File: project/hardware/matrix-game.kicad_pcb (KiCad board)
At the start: 2 copper layers, 100 x 100 mm, 32 parts, among them SW1 button_center, SW2 button_left, SW3 button_down, SW4 button_right, SW5 button_up, U1 NUCLEO-F042K6, U2 MAX7219, U3 DM-OLED096-636

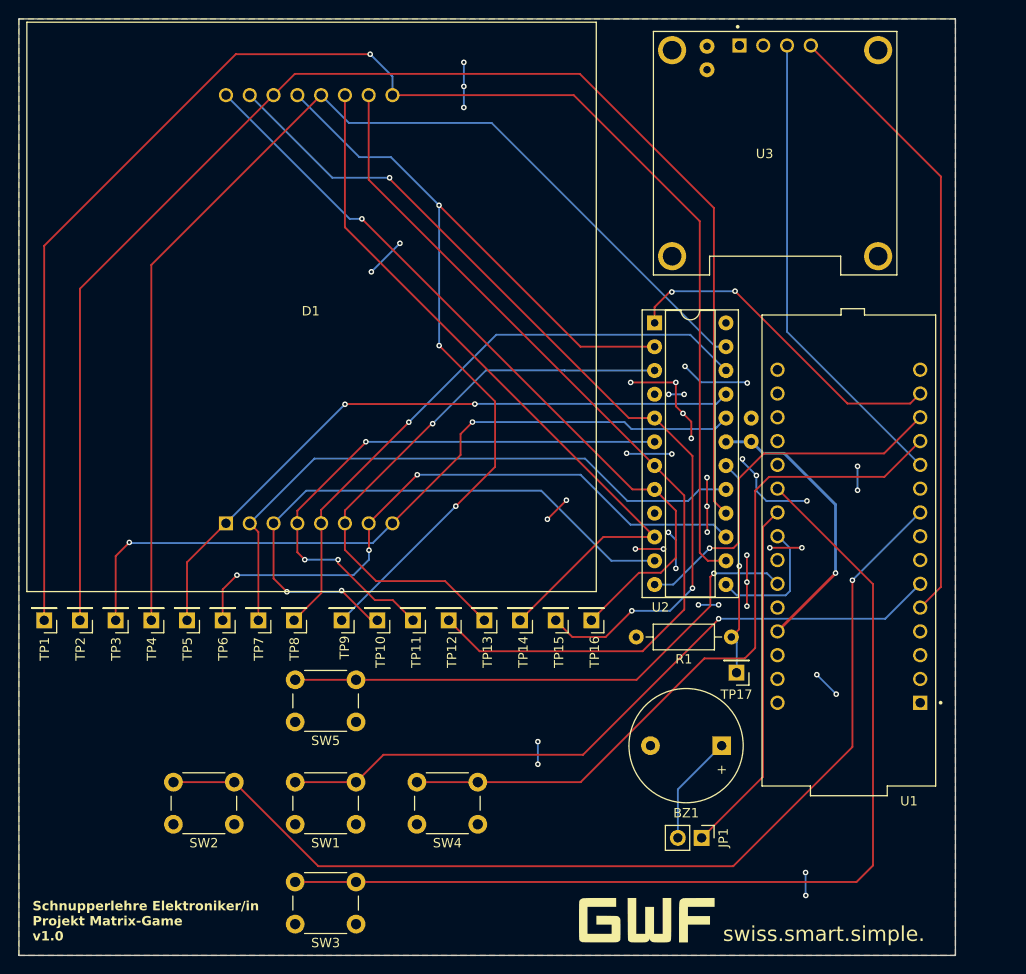
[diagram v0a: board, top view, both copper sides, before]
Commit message: [project/hardware] fix: wrong connection of R1
R1 was wrongly connectet to GND instead of +5V
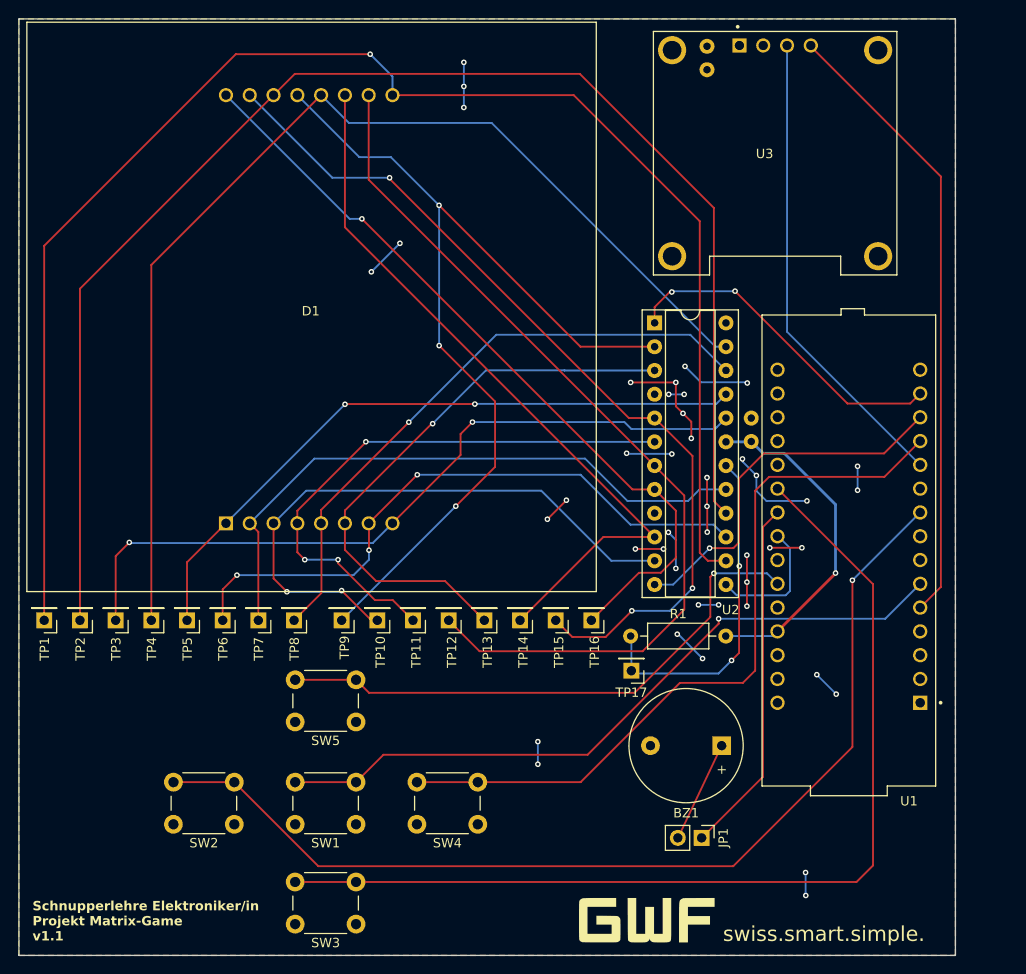
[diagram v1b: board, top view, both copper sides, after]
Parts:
- R1: value 10k -> 22k
- moved TP17 11.2 mm to (155.4, 114.6)
- moved R1 10.8 mm to (155.3, 110.9), turned to 0 degrees
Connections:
- R1 pad 2: GND -> +5V
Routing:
- net Net-(U2-ISET): track 22.7 -> 37.0 mm, vias 1 -> 2
- net Net-(BZ1-+): track 12.3 -> 0.54 mm
- net +5V: track 30.6 -> 36.3 mm
- net GND: track 49.7 -> 53.5 mm, vias 26 -> 28
- net button_up: track 58.5 -> 60.3 mm
- net button_right: track 78.7 -> 80.1 mm
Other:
- board text added: "Schnupperlehre Elektroniker/in Projekt Matrix-Game v1.1"
- board text removed: "Schnupperlehre Elektroniker/in Projekt Matrix-Game v1.0"

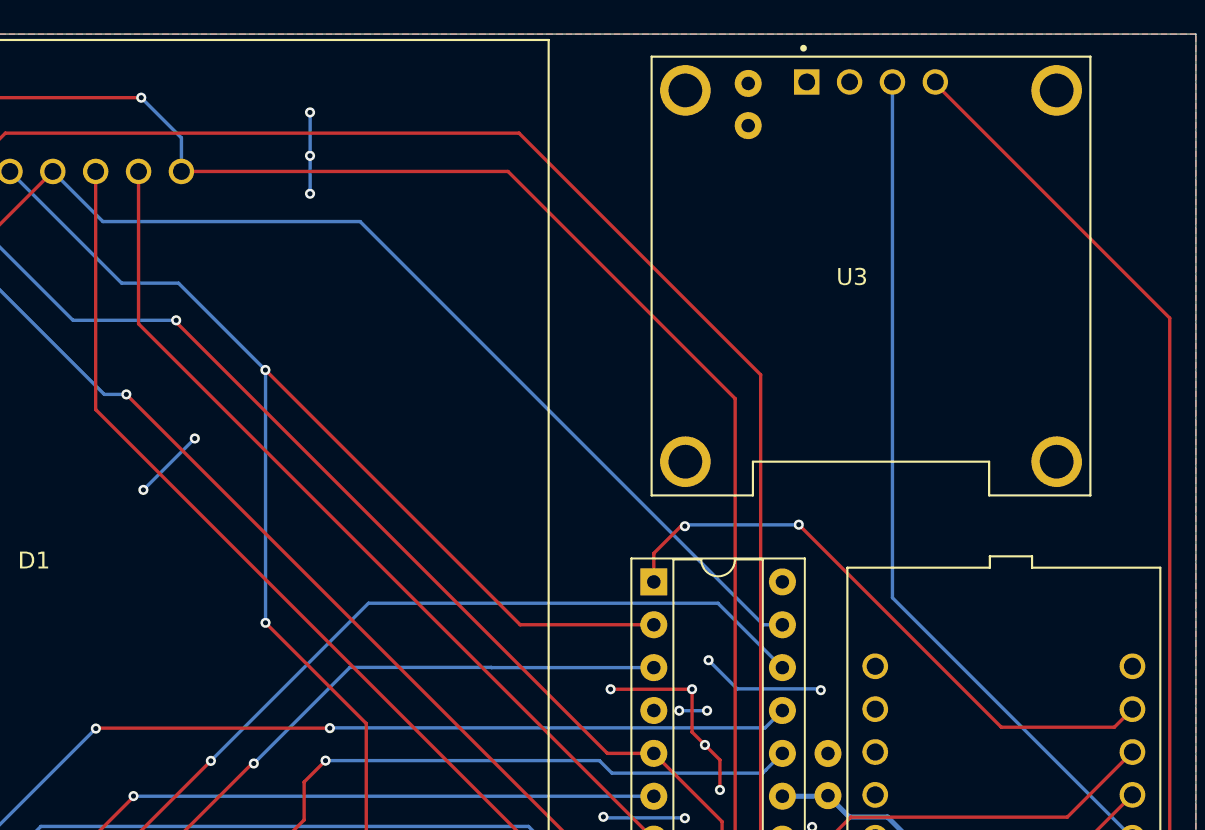
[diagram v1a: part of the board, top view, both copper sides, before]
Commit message: [project/hardware] fix: footprint of LCD
Adjusted mouting hole distances:

- previous[mm]: 22x22
- now[mm]: 23.5x23.8
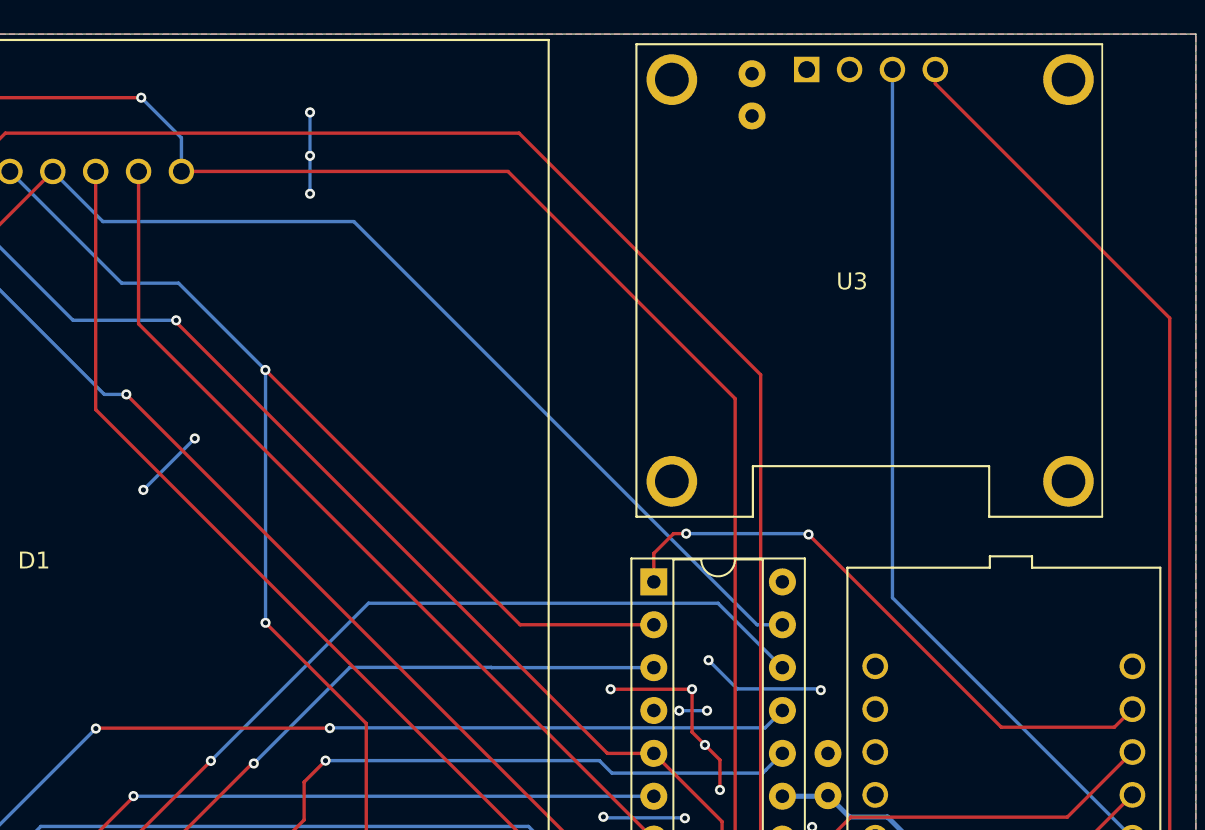
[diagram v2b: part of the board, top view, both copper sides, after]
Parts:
- moved C1 0.62 mm to (163.7, 49.9)
- moved U3 0.26 mm to (170.8, 59.6)
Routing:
- net max_mosi: track 36.4 -> 35.9 mm
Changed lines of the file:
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@@
 	(footprint "DM-OLED096-636:MODULE_DM-OLED096-636"
 		(layer "F.Cu")
-		(at 170.75 59.3375)
+		(at 170.75 59.6)
 		(property "Reference" "U3"
 			(at -1.125 0.0625 0)
@@
 		(attr through_hole)
 		(fp_line
-			(start -13 -13)
-			(end 13 -13)
+			(start -13.9 -14)
+			(end 13.7 -14)
 			(stroke
 				(width 0.127)
@@
 		)
 		(fp_line
-			(start -13 13)
-			(end -13 -13)
+			(start -13.9 14)
+			(end -13.9 -14)
 			(stroke
 				(width 0.127)
@@
 		(fp_line
 			(start -7 11)
-			(end -7 13)
+			(end -7 14)
 			(stroke
 				(width 0.127)
@@
 		)
 		(fp_line
-			(start -7 13)
-			(end -13 13)
+			(start -7 14)
+			(end -13.9 14)
 			(stroke
 				(width 0.127)
@@
 		)
 		(fp_line
-			(start 7 13)
+			(start 7 14)
 			(end 7 11)
 			(stroke
@@
 		)
 		(fp_line
-			(start 13 -13)
-			(end 13 13)
+			(start 13.7 14)
+			(end 7 14)
 			(stroke
 				(width 0.127)
@@
 		)
 		(fp_line
-			(start 13 13)
-			(end 7 13)
+			(start 13.7 14)
+			(end 13.7 -14)
 			(stroke
-				(width 0.127)
-				(type solid)
-			)
-			(layer "F.SilkS")
-		)
-		(fp_circle
-			(center -4 -13.5)
-			(end -3.9 -13.5)
-			(stroke
-				(width 0.2)
-				(type solid)
+				(width 0.1)
+				(type default)
 			)
-			(fill none)
 			(layer "F.SilkS")
 		)
 		(fp_line
-			(start -13.25 -13.25)
-			(end 13.25 -13.25)
+			(start -13.9 -14)
+			(end 13.7 -14)
 			(stroke
 				(width 0.05)
@@
 		)
 		(fp_line
-			(start -13.25 13.25)
-			(end -13.25 -13.25)
+			(start -13.9 14)
+			(end -13.9 -14)
 			(stroke
 				(width 0.05)
@@
 		)
 		(fp_line
-			(start 13.25 -13.25)
-			(end 13.25 13.25)
+			(start 13.7 -14)
+			(end 13.7 14)
 			(stroke
 				(width 0.05)
@@
 		)
 		(fp_line
-			(start 13.25 13.25)
-			(end -13.25 13.25)
+			(start 13.7 14)
+			(end -13.9 14)
 			(stroke
 				(width 0.05)
@@
 		)
 		(fp_line
-			(start -13 -13)
-			(end 13 -13)
+			(start -13.9 -14)
+			(end 13.7 -14)
 			(stroke
 				(width 0.127)
@@
 		)
 		(fp_line
-			(start -13 13)
-			(end -13 -13)
+			(start -13.9 14)
+			(end -13.9 -14)
 			(stroke
 				(width 0.127)
@@
 		)
 		(fp_line
-			(start -7 13)
-			(end -13 13)
+			(start -7 14)
+			(end -13.9 14)
 			(stroke
 				(width 0.127)
@@
 		)
 		(fp_line
-			(start -7 13)
+			(start -7 14)
 			(end -7 11)
 			(stroke
@@
 		(fp_line
 			(start 7 11)
-			(end 7 13)
+			(end 7 14)
 			(stroke
 				(width 0.127)
@@
 		)
 		(fp_line
-			(start 13 -13)
-			(end 13 13)
+			(start 13.7 -14)
+			(end 13.7 14)
 			(stroke
 				(width 0.127)
@@
 		)
 		(fp_line
-			(start 13 13)
-			(end 7 13)
+			(start 13.7 14)
+			(end 7 14)
 			(stroke
 				(width 0.127)
@@
 		)
 		(pad "1" thru_hole rect
-			(at -3.81 -11.5)
+			(at -3.81 -12.5)
 			(size 1.508 1.508)
 			(drill 1)
@@
 		)
 		(pad "2" thru_hole circle
-			(at -1.27 -11.5)
+			(at -1.27 -12.5)
 			(size 1.508 1.508)
 			(drill 1)
@@
 		)
 		(pad "3" thru_hole circle
-			(at 1.27 -11.5)
+			(at 1.27 -12.5)
 			(size 1.508 1.508)
 			(drill 1)
@@
 		)
 		(pad "4" thru_hole circle
-			(at 3.81 -11.5)
+			(at 3.81 -12.5)
 			(size 1.508 1.508)
 			(drill 1)
@@
 		)
 		(pad "S1" thru_hole circle
-			(at -11 -11)
+			(at -11.8 -11.9)
 			(size 3 3)
 			(drill 2)
@@
 		)
 		(pad "S2" thru_hole circle
-			(at 11 -11)
+			(at 11.7 -11.9)
 			(size 3 3)
 			(drill 2)
@@
 		)
 		(pad "S3" thru_hole circle
-			(at 11 11)
+			(at 11.7 11.9)
 			(size 3 3)
 			(drill 2)
@@
 		)
 		(pad "S4" thru_hole circle
-			(at -11 11)
+			(at -11.8 11.9)
 			(size 3 3)
 			(drill 2)
@@
 		(model "${KIPRJMOD}/libs/DM-OLED096-636/DM-OLED096-636.step"
 			(offset
-				(xyz 0 0 8.5)
+				(xyz 0 1 8.5)
 			)
 			(scale
@@
 		(model "${KICAD8_3DMODEL_DIR}/Connector_PinSocket_2.54mm.3dshapes/PinSocket_1x04_P2.54mm_Vertical.step"
 			(offset
-				(xyz 3.9 11.5 0)
+				(xyz 3.8 12.5 0)
 			)
 			(scale
@@
 	(footprint "Capacitor_THT:C_Disc_D3.0mm_W2.0mm_P2.50mm"
 		(layer "B.Cu")
-		(at 163.475 50.425 90)
+		(at 163.7 49.85 90)
 		(descr "C, Disc series, Radial, pin pitch=2.50mm, , diameter*width=3*2mm^2, Capacitor")
 		(tags "C Disc series Radial pin pitch 2.50mm  diameter 3mm width 2mm Capacitor")
@@
 	)
 	(segment
-		(start 164.36863 80)
-		(end 140.47863 56.11)
+		(start 165.5 80)
+		(end 164 80)
 		(width 0.2)
 		(layer "B.Cu")
@@
 	)
 	(segment
-		(start 140.47863 56.11)
+		(start 140.11 56.11)
 		(end 125.24 56.11)
 		(width 0.2)
@@
 	)
 	(segment
-		(start 165.5 80)
-		(end 164.36863 80)
+		(start 164 80)
+		(end 140.11 56.11)
 		(width 0.2)
 		(layer "B.Cu")
@@
 	)
 	(segment
-		(start 185.1695 86.0705)
-		(end 186.24 85)
+		(start 167.05 74.65)
+		(end 178.4705 86.0705)
 		(width 0.2)
 		(layer "F.Cu")
@@
 	)
 	(segment
-		(start 178.4705 86.0705)
-		(end 185.1695 86.0705)
+		(start 185.1695 86.0705)
+		(end 186.24 85)
 		(width 0.2)
 		(layer "F.Cu")
@@
 	)
 	(segment
-		(start 157.88 75.77)
-		(end 157.88 77.46)
+		(start 159.8 74.6)
+		(end 159.05 74.6)
 		(width 0.2)
 		(layer "F.Cu")
@@
 	)
 	(segment
-		(start 159.72 74.16)
-		(end 159.49 74.16)
+		(start 159.05 74.6)
+		(end 157.88 75.77)
 		(width 0.2)
 		(layer "F.Cu")
@@
 	)
 	(segment
-		(start 159.49 74.16)
-		(end 157.88 75.77)
+		(start 157.88 75.77)
+		(end 157.88 77.46)
 		(width 0.2)
 		(layer "F.Cu")
@@
 	)
 	(segment
-		(start 166.47 74.07)
-		(end 178.4705 86.0705)
+		(start 178.4705 86.0705)
+		(end 185.1695 86.0705)
 		(width 0.2)
 		(layer "F.Cu")
@@
 	)
 	(via
-		(at 159.72 74.16)
+		(at 159.8 74.6)
 		(size 0.6)
 		(drill 0.3)
@@
 	)
 	(via
-		(at 166.47 74.07)
+		(at 167.05 74.65)
 		(size 0.6)
 		(drill 0.3)
@@
 	)
 	(segment
-		(start 159.8 74.08)
-		(end 159.72 74.16)
-		(width 0.2)
-		(layer "B.Cu")
-		(net 44)
-	)
-	(segment
-		(start 166.47 74.07)
-		(end 166.46 74.08)
+		(start 167.05 74.65)
+		(end 167 74.6)
 		(width 0.2)
 		(layer "B.Cu")
@@
 	)
 	(segment
-		(start 159.72 74.16)
-		(end 159.89 73.99)
+		(start 159.8 74.6)
+		(end 159.7 74.5)
 		(width 0.127)
 		(layer "B.Cu")
@@
 	)
 	(segment
-		(start 166.46 74.08)
-		(end 159.8 74.08)
+		(start 167 74.6)
+		(end 159.8 74.6)
 		(width 0.2)
 		(layer "B.Cu")
